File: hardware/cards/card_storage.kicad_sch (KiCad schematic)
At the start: 22 parts, among them J1 Conn_02x20_Odd_Even, J2 Conn_02x25_Odd_Even, U1 74HCT04, U10 74HCT573, U11 74HCT138, U2 74HCT08, U3 74HCT08, U4 74HCT32, U5 74HCT125, U6 74HCT138, U7 74HCT138, U8 74HCT245, U9 74HCT573

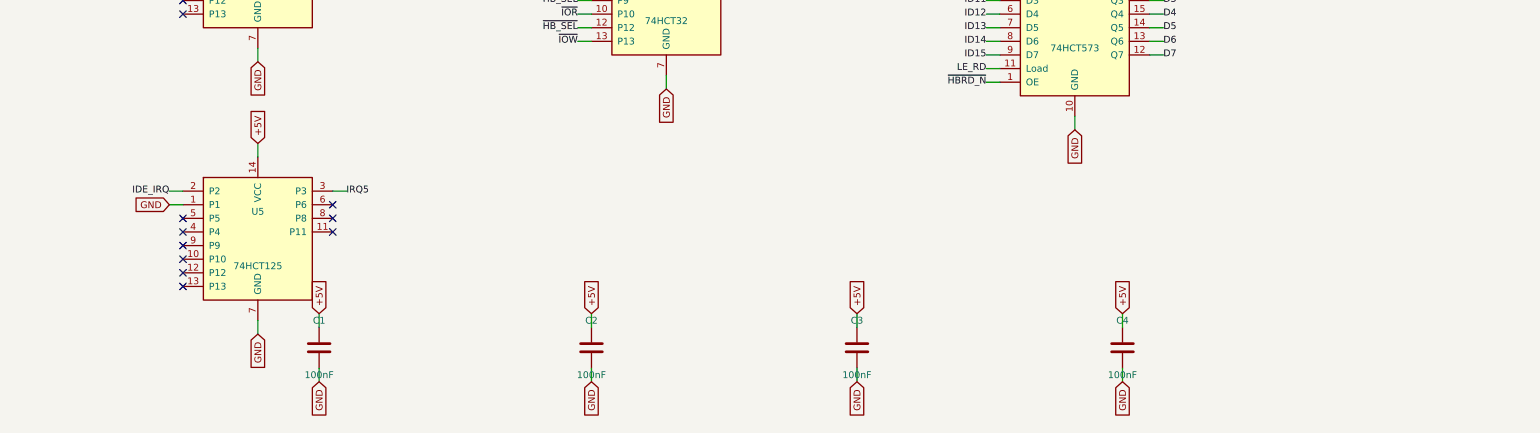
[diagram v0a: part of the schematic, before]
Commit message: Design review 2026-07-11: rail protection, decoupling, wiring fixes
Protection:
- Sidecar +5V now feeds through a 2A polyfuse into +5V_ISA with an
  SMBJ5.0A clamp + 22uF bulk (a faulted ISA card trips its own fuse
  instead of dropping the board; back-fed voltage is clamped).
- USB-C VBUS enters through a 3A polyfuse with an SMBJ5.0A on +5V
  (backstop for the CFG1 9-20V failure mode). CH224K gains a 1uF VDD
  cap; its PG routes to Supervisor GPIO16 as PD_PG. Buck output
  doubled to 2x22uF, 10uF at VIN, extra rail bulk.
- Supervisor USB-A host port: 27R series termination (RP2040
  requirement), USBLC6-2SC6 ESD array, 100uF VBUS bulk.
- Video: HDMI +5V fused (500mA), HPD sensed on GPIO41, 100R series on
  VGA sync. TMDS ESD array deferred to layout (no symbol).
- card_isatest: V5RAW bulk, Q1 gate soft-start cap, TVS on DUT rail.

Wiring fixes:
- SPKR had no driver anywhere (netlist: 1 node). Bus MCU GPIO22
  reassigned from the diagnostics-only bus-CLK sense to SPKR; bus_mcu
  drops CLK from its interface. Doc 5.2 updated.
- bus_mcu C8 decoupled +3V3, a rail that sheet never uses -> 3V3_BUS.
- Storage IRQ5 was push-pull (permanently driven when idle) -> 2N7002
  + gated '125 tri-state, same convention as the LPT IRQ7 stage.
- MAX3241 pump caps resized to the 5V datasheet values (47nF/330nF).
- LPT DB25 status inputs get 4.7k pull-ups (floated with no printer).
- Audio line-out gets a 100R series isolator before the jack.

Best practices:
- Decoupling to ~1x100nF per IC on every sheet + bulk per board
  (cpu_core 7->16 incl. the naked 3.3V oscillator, storage 4->11,
  parallel 6->13, rtc/com/video/bus_mcu/card_isatest similar).
- All floating spare CMOS inputs tied ('00/'74/'157/'02/'04/'125
  sections across cpu_core, bus_mcu, rtc, storage, card_isatest).

Sourcing: new parts mapped in parts.py with JLC-verified LCSC numbers;
Power_Protection lib registered in the tools; TPS563200 stock alert
(4 pcs left at JLC) flagged in parts.py + jlcpcb-sourcing.md. All
decisi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
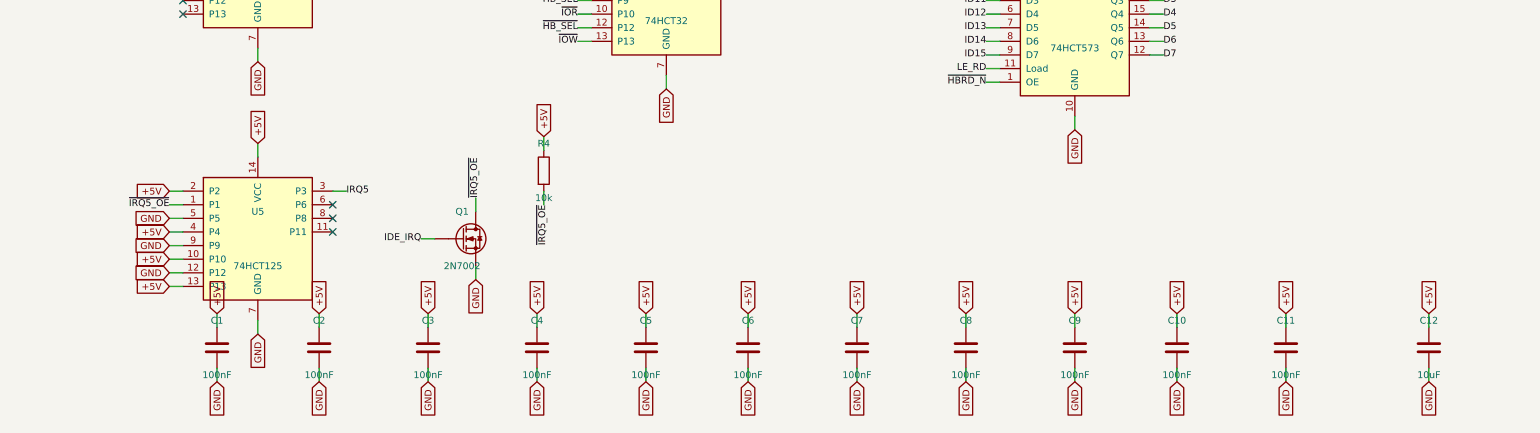
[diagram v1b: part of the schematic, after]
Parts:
- added C10, C11, C5, C6, C7, C8, C9: 100nF, symbol Device:C
- added C12: 10uF, symbol Device:C
- added Q1: 2N7002, symbol Device:Q_NMOS
- added R4: 10k, symbol Device:R
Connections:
- net +5V: now also U5.10 (P10), U5.13 (P13), U5.2 (P2), U5.4 (P4), C10.1, C11.1, C12.1, C5.1, C6.1, C7.1, C8.1, C9.1, R4.1
- net GND: now also U5.12 (P12), U5.5 (P5), U5.9 (P9), C10.2, C11.2, C12.2, C5.2, C6.2, C7.2, C8.2, C9.2, Q1.S; no longer U5.1 (P1)
- net IDE_IRQ: now also Q1.G; no longer U5.2 (P2)
- new net ~{IRQ5_OE}: Q1.D, R4.2, U5.1 (P1)
- no-connect marks 46 -> 40

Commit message: Storage/video: enable + base-address straps
Completes the jumper story started with COM/LPT: every on-board peripheral
can now be disabled or re-strapped to make room for the same card on the
sidecar chain.

- storage: JP1 base 0x300/0x320 (differ only in A5; A5_SEL replaces nA5 in
  the HI_MATCH tree, XTIDE UB supports both) and JP2 enable on DEC1's spare
  ~E1 (open kills /CS0 + /ODD_SEL, so DEC2/DEC3, both high-byte latches and
  the low-byte '245 go inert; INTRQ's pull-down keeps IRQ5 released). Same
  pattern as the LPT sheet.
- video: firmware-read boot straps -- this snoop card decodes in firmware,
  so there is no hardware chip-select to gate. JP1/VID_EN (GPIO42, 10k to
  3V3_VID) open = firmware keeps every bus-facing OE off (all drivers are
  MCU-gated tri-states, so a disabled card is electrically silent);
  JP2/VID_BASE (GPIO43) closed = CGA windows (0x3D4/0xB8000), open =
  MDA/Hercules (0x3B4/0xB0000) -- the snoop equivalent of a period card's
  MDA/CGA switch.

Design doc updated (8, 10, 14 I/O map); decisions logged in
questions-storage.md / questions-video.md.

Verified: motherboard + cards rebuild with zero structural ERC; netlist
ties each strap to its jumper, pull resistor and decode/GPIO pin
(A5_SEL/~{STOR_EN} on storage, VID_EN/VID_BASE on the video module).

Co-Authored-By: Claude Fable 5 <noreply@anthropic.com>
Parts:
- added C1: 100nF, symbol Device:C
- added JP2: STOR_EN, symbol Connector_Generic:Conn_01x02
- added R5: 10k, symbol Device:R
- JP1: renamed from C1; value 100nF -> BASE 300/320; symbol Device:C -> Connector_Generic:Conn_01x03; LCSC Part Num C14663 -> C2337
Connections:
- net +5V: now also C1.1, R5.1; no longer JP1.1
- net A5: now also JP1.3 (Pin_3)
- net GND: now also C1.2, JP2.2 (Pin_2); no longer JP1.2, U6.5 (~{E1})
- net nA5: now also JP1.1 (Pin_1); no longer U2.4 (P4)
- new net A5_SEL: JP1.2 (Pin_2), U2.4 (P4)
- new net ~{STOR_EN}: JP2.1 (Pin_1), R5.2, U6.5 (~{E1})
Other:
- note added: "JP1 base 0x300/0x320 (XTIDE UB supports both); JP2 open = card disabled."
